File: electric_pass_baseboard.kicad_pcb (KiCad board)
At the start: 2 copper layers, 50 x 100 mm, 129 parts, among them J1 USB_C_Receptacle_USB2.0_16P, J2 Conn_02x05_Odd_Even, J3 Conn_02x05_Odd_Even, J6 Conn_01x02, Q1 AO3401A, SW1 MSK12C02, SW3 TS24CA, SW4 TS24CA, SW5 TS24CA, SW6 TS24CA, SW7 TS24CA, SW8 TS24CA, SW9 TS24CA, U1 TP4056-42-ESOP8, U2 EA3036C, U3 F1C100S, U4 3寸液晶屏TFT 全新无定义资料, U5 E103-RTL8189FTV_C42411897, U6 W25N01GVZEIG_C907680, U7 LSM6DS3, U9 STI9287C, Y1 24Mhz 12pF

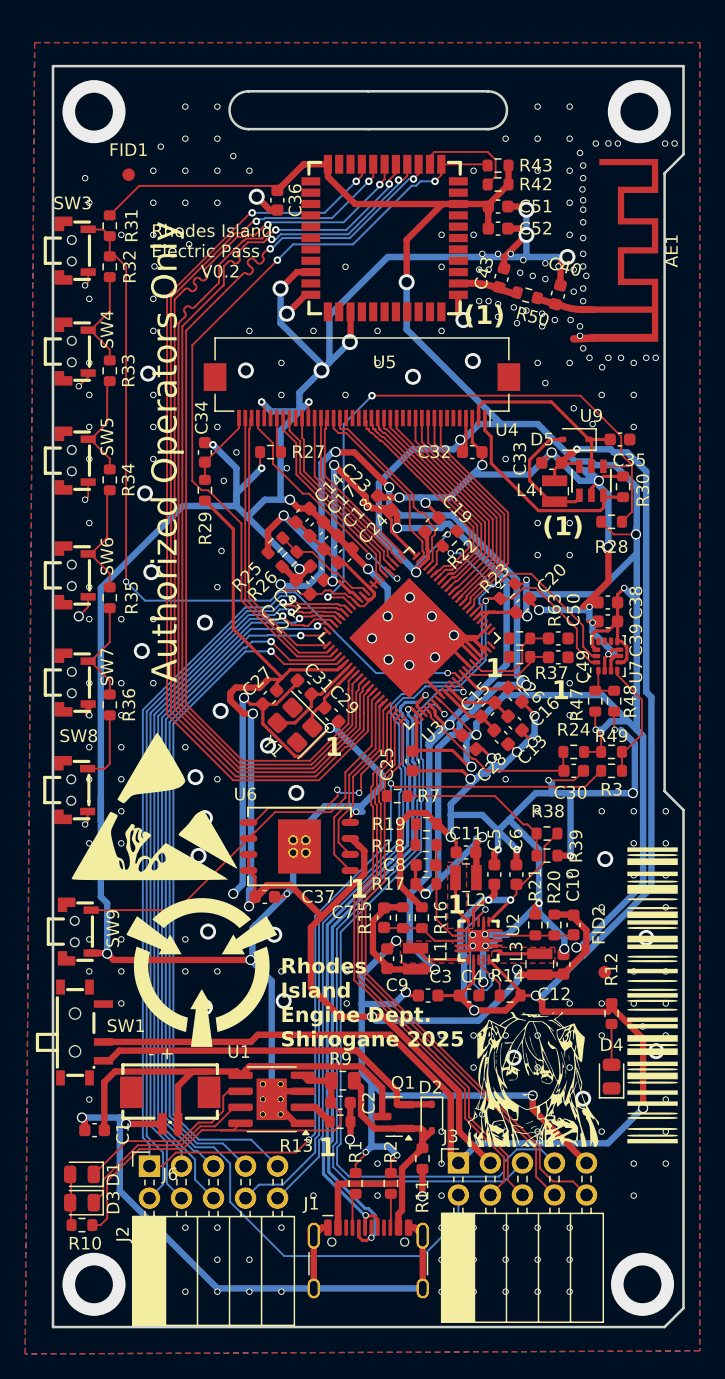
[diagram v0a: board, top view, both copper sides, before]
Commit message: V0.3.1 bugfix
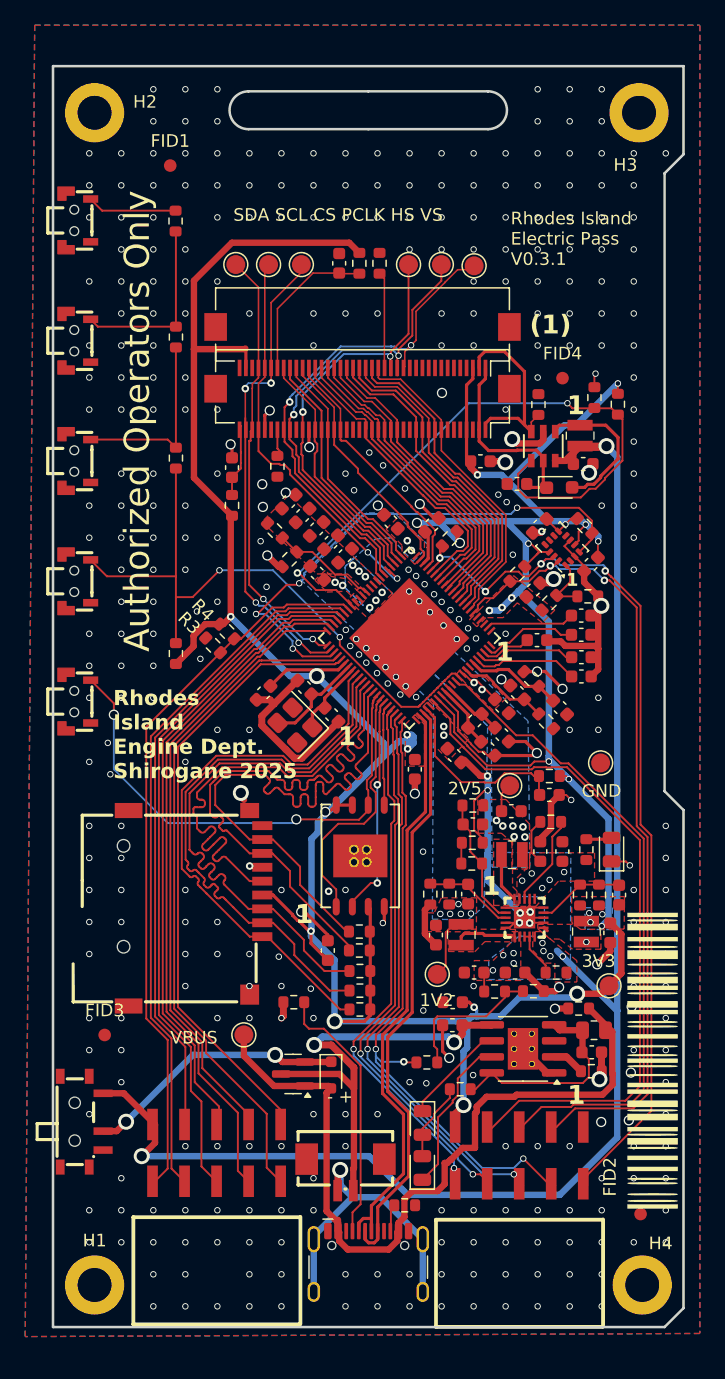
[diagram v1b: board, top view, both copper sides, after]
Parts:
- removed AE1: Antenna_Chip, shirogane:ESPRESSIF_ESP32_MIFA_2.4GHz_LEFT
- removed C51: 100nF, Capacitor_SMD:C_0603_1608Metric
- removed C52: 1uF, Capacitor_SMD:C_0603_1608Metric
- removed the G*** at (131.8, 106.5)
- removed the G*** at (135.5, 119.8)
- removed the G*** at (161.5, 128.2)
- removed the G*** at (159.5, 67.2)
- removed the G*** at (135.2, 122.8)
- removed J6: Conn_01x02, EasyEDA:CONN-SMD_2P-P1.25_XUNPU_WAFER-MX1.25-2PWB
- removed R32: 10K, Resistor_SMD:R_0603_1608Metric
- removed R50: 0R, Resistor_SMD:R_0603_1608Metric
- removed SW3, SW7, SW8: TS24CA, EasyEDA:SW-SMD_TS24CA
- added C41: 1uF, Capacitor_SMD:C_0603_1608Metric, F.Cu at (165.6, 93.0)
- added C42: 1uF, Capacitor_SMD:C_0603_1608Metric, F.Cu at (162.1, 93.4)
- added C44: 1uF, Capacitor_SMD:C_0603_1608Metric, F.Cu at (165.6, 96.3)
- added C45: 100nF, Capacitor_SMD:C_0603_1608Metric, F.Cu at (145.5, 118.0)
- added Card1: TF-115-BCP9, EasyEDA:TF-SMD_TF-115-BCP9, F.Cu at (135.0, 114.7)
- added FID3: Fiducial, Fiducial:Fiducial_1mm_Mask2mm, F.Cu at (127.8, 124.7)
- added FID4: Fiducial, Fiducial:Fiducial_1mm_Mask2mm, F.Cu at (164.1, 72.6)
- added G***: LOGO, shirogane:PRTS, B.Cu at (159.7, 69.8)
- added H1: MountingHole_Pad, MountingHole:MountingHole_2.7mm_M2.5_DIN965_Pad, F.Cu at (127.0, 144.5)
- added H2: MountingHole_Pad, MountingHole:MountingHole_2.7mm_M2.5_DIN965_Pad, F.Cu at (127.0, 51.6)
- added H3: MountingHole_Pad, MountingHole:MountingHole_2.7mm_M2.5_DIN965_Pad, F.Cu at (170.2, 51.6)
- added H4: MountingHole_Pad, MountingHole:MountingHole_2.7mm_M2.5_DIN965_Pad, F.Cu at (170.4, 144.5)
- added R4: 10K, Resistor_SMD:R_0603_1608Metric, F.Cu at (137.5, 92.7)
- added R40: 0R, Resistor_SMD:R_0603_1608Metric, F.Cu at (153.3, 126.9)
- added R41: 10K, Resistor_SMD:R_0603_1608Metric, F.Cu at (149.6, 63.5)
- added R44: 10K, Resistor_SMD:R_0603_1608Metric, F.Cu at (133.4, 60.1)
- added R5: 10K, Resistor_SMD:R_0603_1608Metric, F.Cu at (148.0, 116.5)
- added R6: 10K, Resistor_SMD:R_0603_1608Metric, F.Cu at (148.0, 118.0)
- added R8: 10K, Resistor_SMD:R_0603_1608Metric, F.Cu at (148.0, 119.6)
- added SW2: TS24CA, EasyEDA:SW-SMD_TS24CA, F.Cu at (125.7, 60.1)
- added TP1: TestPoint, TestPoint:TestPoint_Pad_D1.5mm, F.Cu at (154.2, 119.9)
- added TP10: TestPoint, TestPoint:TestPoint_Pad_D1.5mm, F.Cu at (154.5, 63.6)
- added TP11: TestPoint, TestPoint:TestPoint_Pad_D1.5mm, F.Cu at (138.8, 124.7)
- added TP2: TestPoint, TestPoint:TestPoint_Pad_D1.5mm, F.Cu at (159.9, 104.9)
- added TP3: TestPoint, TestPoint:TestPoint_Pad_D1.5mm, F.Cu at (167.8, 120.8)
- added TP4: TestPoint, TestPoint:TestPoint_Pad_D1.5mm, F.Cu at (143.4, 63.6)
- added TP5: TestPoint, TestPoint:TestPoint_Pad_D1.5mm, F.Cu at (138.2, 63.6)
- added TP6: TestPoint, TestPoint:TestPoint_Pad_D1.5mm, F.Cu at (167.1, 103.1)
- added TP7: TestPoint, TestPoint:TestPoint_Pad_D1.5mm, F.Cu at (140.8, 63.6)
- added TP8: TestPoint, TestPoint:TestPoint_Pad_D1.5mm, F.Cu at (151.9, 63.6)
- added TP9: TestPoint, TestPoint:TestPoint_Pad_D1.5mm, F.Cu at (157.1, 63.7)
- added U8: WAFER-MX1.25-2PWB, EasyEDA:CONN-SMD_2P-P1.25_XUNPU_WAFER-MX1.25-2PWB, F.Cu at (146.9, 135.8)
- C40, C43: value TBD -> 1uF
- J2, J3: value Conn_02x05_Odd_Even -> Conn_02x05_Counter_Clockwise; footprint Connector_PinSocket_2.54mm:PinSocket_2x05_P2.54mm_Horizontal -> EasyEDA:HDR-SMD_10P-P2.54-H-F-R2-C5-W8.5
- R3, R7: value 0R -> 10K
- R38, R39: value 47K -> 68K
- R42, R43: value 68K -> 10K
- U3: value F1C100S -> F1C200S
- U4: value 3寸液晶屏TFT 全新无定义资料 -> FPC 0.5mm 40P 下接
- U5: value E103-RTL8189FTV_C42411897 -> FPC 0.5mm 40P 上接; footprint EasyEDA:WIRELM-SMD_E103-RTL8189FTV -> Connector_FFC-FPC:Hirose_FH12-40S-0.5SH_1x40-1MP_P0.50mm_Horizontal
- moved R43 52.2 mm to (163.2, 107.8), turned to 0 degrees
- moved R35 36.9 mm to (148.0, 121.2), turned to 0 degrees
- moved R7 35.3 mm to (166.6, 74.2), turned to 90 degrees
- moved R31 34.3 mm to (133.4, 94.5), turned to -90 degrees
- moved R3 33.1 mm to (136.4, 93.8), turned to -45 degrees
- moved R10 31.9 mm to (156.0, 129.0)
- moved R36 31.3 mm to (148.0, 122.7), turned to 0 degrees
- moved C43 30.7 mm to (165.6, 94.7), turned to 180 degrees
- moved C1 29.6 mm to (155.4, 123.9)
- moved D1 27.3 mm to (153.0, 131.7), turned to -90 degrees
- moved D3 27.1 mm to (153.0, 135.2), turned to 90 degrees
- moved C40 25.5 mm to (165.6, 91.4), turned to 180 degrees
- moved C2 20.3 mm to (166.4, 126.1)
- moved R13 20.3 mm to (166.4, 127.6)
- moved R9 20.3 mm to (166.6, 124.3)
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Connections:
- net /GPADC2 renamed /ADC
- net /screen/SCR_RST renamed Net-(U4-RESET)
- net /soc_f1c/USB_DM renamed /USB_DN
- net /soc_f1c/USB_DP renamed /USB_DP
- C36 pad 1: +3.3V -> Net-(U5-RESET)
- C40 pad 1: Net-(AE1-PCB_Trace) -> GND
- C40 pad 2: GND -> Net-(U3-HPCOMFB)
- C43 pad 1: /rtl8189ftv/WIFI_ANT -> GND
- C43 pad 2: GND -> Net-(U3-FMINR)
- J2 pad 1: /TWI0_IRQ -> /UART0_RX
- J2 pad 10: /TWI0_SDA -> /UART0_TX
- J2 pad 2: /SPI1_MISO -> /PE5
- J2 pad 5: /PE6 -> VBAT_OUT
- J2 pad 6: /SPI1_MOSI -> /PE11
- J2 pad 7: /UART0_TX -> /SPI1_MISO
- J2 pad 8: /TWI0_SCL -> /SPI1_MOSI
- J2 pad 9: /UART0_RX -> /PE6
- J3 pad 1: VBAT_OUT -> GND
- J3 pad 10: /GPADC1 -> /TWI0_SCL
- J3 pad 2: /PE5 -> /TWI0_SDA
- J3 pad 3: +3.3V -> /TVIN0
- J3 pad 4: /GPADC4 -> /TVOUT
- J3 pad 5: /TVIN0 -> +3.3V
- J3 pad 6: /GPADC3 -> /UART1_TX
- J3 pad 7: /TVOUT -> /UART1_RX
- J3 pad 9: GND -> /VBAT_SENSE
- R3 pad 1: /TWI0_IRQ -> GND
- R3 pad 2: /soc_peripherals/IMU_IRQ -> /PE11
- R33 pad 2: Net-(R32-Pad1) -> /adc_periph/ADCBTN_OUT
- R35 pad 1: Net-(R35-Pad1) -> /soc_f1c/SDIO_D3
- R35 pad 2: Net-(R34-Pad1) -> +3.3V
- R36 pad 1: Net-(R36-Pad1) -> /soc_f1c/SDIO_D2
- R36 pad 2: Net-(R35-Pad1) -> +3.3V
- R42 pad 1: +3.3V -> Net-(U5-RESET)
- R42 pad 2: Net-(U5-WAKEHOST) -> +3.3V
- R43 pad 1: +3.3V -> VBAT_OUT
- R43 pad 2: /rtl8189ftv/WIFI_EN -> Net-(U2-EN3)
- R49 pad 1: /soc_peripherals/IMU_IRQ -> /soc_f1c/I2C_IRQ
- R7 pad 1: /GPADC1 -> /screen/SCREEN_BL_CTRL
- R7 pad 2: /adc_periph/ADCBAT -> GND
- SW1 pad 1: unconnected-(SW1-Pad1) -> VBAT_OUT
- SW1 pad 2: VBAT_OUT -> Net-(D2-K)
- SW1 pad 3: Net-(D2-K) -> unconnected-(SW1-Pad3)
- SW4 pad 4: Net-(R32-Pad1) -> /adc_periph/ADCBTN_OUT
- U2 pad 18: Net-(U2-EN1) -> Net-(U2-EN3)
- U3 pad 2: GND -> Net-(U3-HPCOMFB)
- U3 pad 38: /TWI0_IRQ -> /PE11
- U3 pad 47: /rtl8189ftv/WIFI_EN -> /soc_f1c/I2C_IRQ
- U3 pad 53: /rtl8189ftv/SDIO_D2 -> /soc_f1c/SDIO_D2
- U3 pad 54: /rtl8189ftv/SDIO_D3 -> /soc_f1c/SDIO_D3
- U3 pad 55: /rtl8189ftv/SDIO_CMD -> /soc_f1c/SDIO_CMD
- U3 pad 56: /rtl8189ftv/SDIO_CLK -> /soc_f1c/SDIO_CLK
- U3 pad 57: /rtl8189ftv/SDIO_D0 -> /soc_f1c/SDIO_D0
- U3 pad 58: /rtl8189ftv/SDIO_D1 -> /soc_f1c/SDIO_D1
- U3 pad 63: /GPADC4 -> /UART1_TX
- U3 pad 64: /GPADC3 -> /UART1_RX
- U3 pad 66: /GPADC1 -> /VBAT_SENSE
- U3 pad 84: GND -> Net-(U3-FMINL)
- U3 pad 85: GND -> Net-(U3-FMINR)
- U3 pad 86: GND -> Net-(U3-LINL)
- U3 pad 87: GND -> Net-(U3-MICIN)
- U5 pad 1: GND -> /screen/SCREEN_LED_A
- U5 pad 10: unconnected-(U5-NC-Pad10) -> GND
- U5 pad 11: unconnected-(U5-NC-Pad11) -> GND
- U5 pad 12: /rtl8189ftv/WIFI_EN -> GND
- U5 pad 13: Net-(U5-WAKEHOST) -> GND
- U5 pad 14: /rtl8189ftv/SDIO_D2 -> /screen/SCREEN_VS
- U5 pad 15: /rtl8189ftv/SDIO_D3 -> /screen/SCREEN_HS
- U5 pad 16: /rtl8189ftv/SDIO_CMD -> /screen/SCREEN_PCLK
- U5 pad 17: /rtl8189ftv/SDIO_CLK -> Net-(U5-DEN)
- U5 pad 18: /rtl8189ftv/SDIO_D0 -> /screen/SCREEN_R0
- U5 pad 19: /rtl8189ftv/SDIO_D1 -> /screen/SCREEN_R1
- U5 pad 2: /rtl8189ftv/WIFI_ANT -> /screen/SCREEN_LED_K
- U5 pad 20: GND -> /screen/SCREEN_R2
- U5 pad 21: unconnected-(U5-NC-Pad21) -> /screen/SCREEN_R3
- U5 pad 22: +3.3V -> /screen/SCREEN_R4
- U5 pad 23: unconnected-(U5-NC-Pad23) -> /screen/SCREEN_G0
- U5 pad 24: unconnected-(U5-NC-Pad24) -> /screen/SCREEN_G1
- U5 pad 25: unconnected-(U5-NC-Pad25) -> /screen/SCREEN_G2
- U5 pad 26: unconnected-(U5-NC-Pad26) -> /screen/SCREEN_G3
- U5 pad 27: unconnected-(U5-NC-Pad27) -> /screen/SCREEN_G4
- U5 pad 28: unconnected-(U5-NC-Pad28) -> /screen/SCREEN_G5
- U5 pad 29: unconnected-(U5-NC-Pad29) -> /screen/SCREEN_B0
- U5 pad 3: GND -> +3.3V
- U5 pad 30: unconnected-(U5-NC-Pad30) -> /screen/SCREEN_B1
- U5 pad 31: GND -> /screen/SCREEN_B2
- U5 pad 32: unconnected-(U5-NC-Pad32) -> /screen/SCREEN_B3
- U5 pad 33: GND -> /screen/SCREEN_B4
- U5 pad 34: unconnected-(U5-NC-Pad34) -> Net-(U5-RESET)
- U5 pad 35: unconnected-(U5-NC-Pad35) -> /screen/SCREEN_CS
- U5 pad 36: GND -> /screen/SCREEN_SCL
- U5 pad 37: unconnected-(U5-NC-Pad37) -> /screen/SCREEN_SDA
- U5 pad 38: unconnected-(U5-NC-Pad38) -> GND
- U5 pad 39: unconnected-(U5-NC-Pad39) -> +3.3V
- U5 pad 4: unconnected-(U5-NC-Pad4) -> GND
- U5 pad 40: unconnected-(U5-NC-Pad40) -> GND
- U5 pad 5: unconnected-(U5-NC-Pad5) -> GND
- U5 pad 6: unconnected-(U5-NC-Pad6) -> GND
- U5 pad 7: unconnected-(U5-NC-Pad7) -> GND
- U5 pad 8: unconnected-(U5-NC-Pad8) -> GND
- U5 pad 9: +3.3V -> GND
- U7 pad 4: /soc_peripherals/IMU_IRQ -> /soc_f1c/I2C_IRQ
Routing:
- net GND: track 624.8 -> 157.5 mm, vias 324 -> 382
- net /TWI0_IRQ: track 118.7 -> 0.00 mm, vias 3 -> 0
- net +2V5: track 117.4 -> 5.72 mm, vias 7 -> 14
- net +1V2: track 95.2 -> 5.09 mm, vias 5 -> 11
- net /rtl8189ftv/SDIO_CLK: track 77.8 -> 0.00 mm, vias 2 -> 0
- net /rtl8189ftv/SDIO_D1: track 76.5 -> 0.00 mm, vias 2 -> 0
- net /rtl8189ftv/SDIO_CMD: track 76.4 -> 0.00 mm, vias 2 -> 0
- net /rtl8189ftv/SDIO_D0: track 76.3 -> 0.00 mm, vias 2 -> 0
- net /rtl8189ftv/SDIO_D3: track 76.3 -> 0.00 mm, vias 2 -> 0
- net /rtl8189ftv/SDIO_D2: track 75.9 -> 0.00 mm, vias 2 -> 0
- net /rtl8189ftv/WIFI_EN: track 61.4 -> 0.00 mm, vias 2 -> 0
- net /PE11: track 0.00 -> 57.4 mm
- net /VBAT_SENSE: track 0.00 -> 50.6 mm, vias 0 -> 3
- net /GPADC1: track 47.0 -> 0.00 mm
- net +3.3V: track 347.3 -> 300.5 mm, vias 16 -> 27
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- added copper zone on B.Cu, net +1V2
- added copper zone on F.Cu, net +1V2
- added copper zone on B.Cu, net +2V5
- added copper zone on F.Cu, net +2V5
- added copper zone on B.Cu, net +3.3V
- added copper zone on F.Cu, net +3.3V
- added copper zone on B.Cu, net VBAT_OUT
- added copper zone on F.Cu, net VBAT_OUT
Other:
- board text added: "1 2 3 4 FEL"
- board text added: "1V2"
- board text added: "2V5"
- board text added: "3V3"
- board text added: "Electronic Authorization Terminal 电子通行证终端 Model/型号: EPA-V031 Power/电源: 5V1A ACC ID: 429a12 LMIIT ID: 7355608 拉特兰机械制造总局受托制造"
- board text added: "GND"
- board text added: "GND SDA TVI TVO 3V3 SCL AD1 AD2 AD3 AD4"
- board text added: "ON OFF"
- board text added: "Rhodes Island Electric Pass"
- board text added: "Rhodes Island Electric Pass V0.3.1"
- board text added: "SDA SCL CS PCLK HS VS"
- board text added: "URX PE5 CS SCK BAT UTX PE6 MOS MIS E11"
- board text added: "VBUS"
- board text removed: "Electronic Authorization Terminal 电子通行证终端 Model/型号: EPA-V01 Power/电源: 5V1A FCC ID: 429473 LMIIT ID: 23819AU98 拉特兰机械制造总局受托制造"
- board text removed: "GND TVO TVI 3V3 BAT AD1 AE2 AD3 AD4 PE5"
- board text removed: "Rhodes Island Electric Pass V0.2"
- board text removed: "Rhodes Island Pass"
- board text removed: "URX UTX PE6 CS IRQ SDA SCL MSI SCK MSO"
